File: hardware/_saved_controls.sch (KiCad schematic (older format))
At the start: 25 parts, among them J301 PJ301M-12, J302 PJ301M-12, J303 PJ301M-12, J304 PJ301M-12, U301 MCP6004

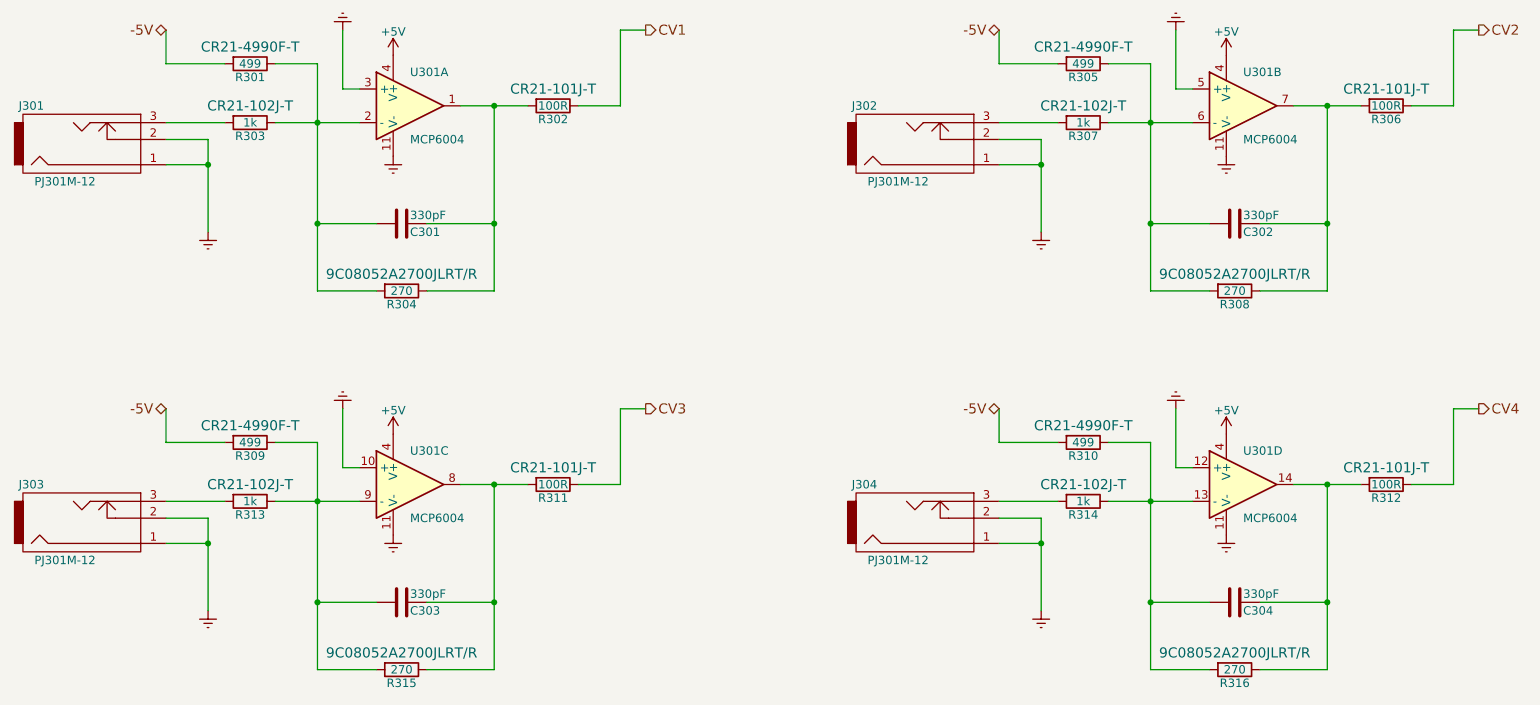
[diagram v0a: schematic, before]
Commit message: jacks on a different sheet than the buffers. single PCB with jumpers and mouse bites
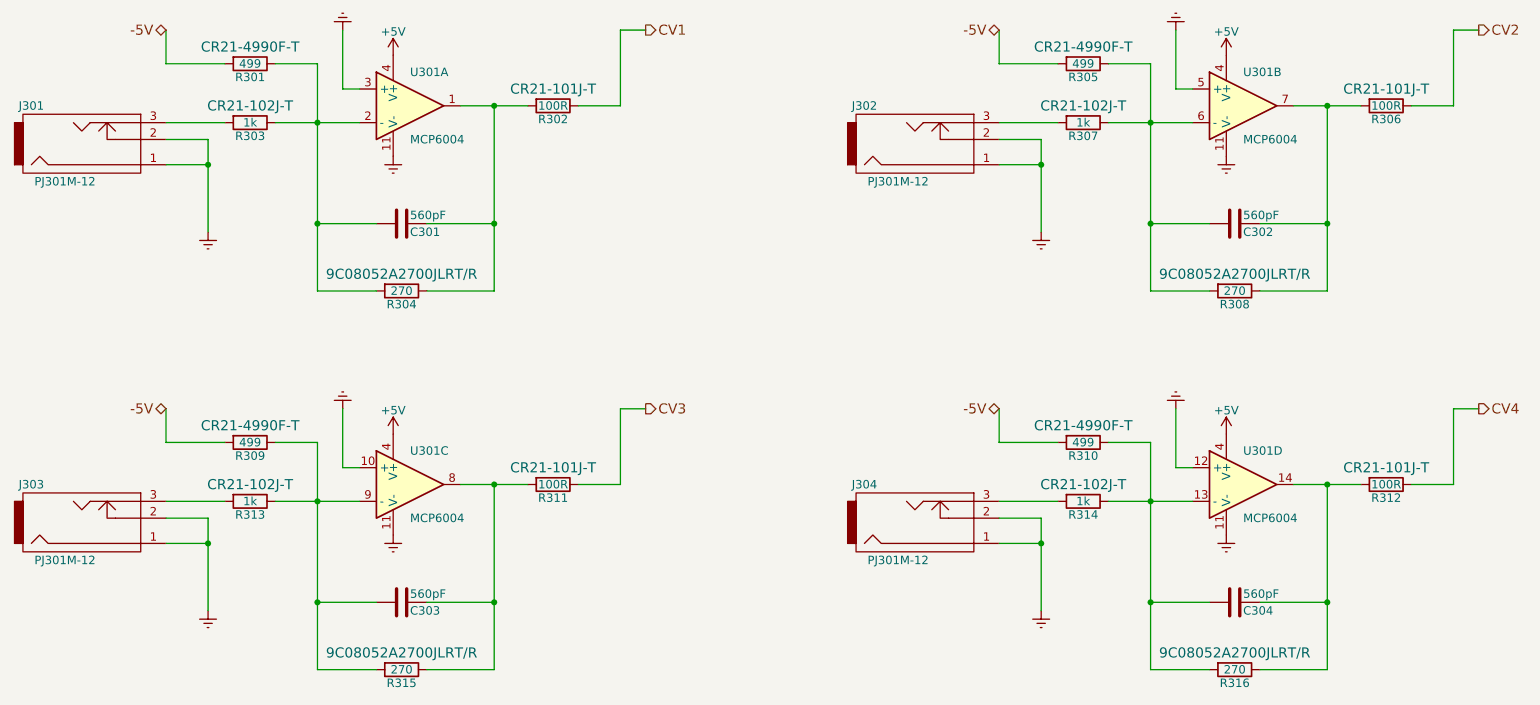
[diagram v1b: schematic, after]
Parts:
- C301, C302, C303, C304: value 330pF -> 560pF; footprint (none) -> Capacitors_THT:C_Axial_L3.8mm_D2.6mm_P7.50mm_Horizontal
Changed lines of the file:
@@
 P 3400 2300
 F 0 "C301" V 3450 2350 50  0000 L CNN
-F 1 "330pF" V 3350 2350 50  0000 L CNN
-F 2 "" H 3438 2150 50  0000 C CNN
+F 1 "560pF" V 3350 2350 50  0000 L CNN
+F 2 "Capacitors_THT:C_Axial_L3.8mm_D2.6mm_P7.50mm_Horizontal" H 3438 2150 50  0001 C CNN
 F 3 "" H 3400 2300 50  0000 C CNN
 	1    3400 2300
@@
 P 8350 2300
 F 0 "C302" V 8400 2350 50  0000 L CNN
-F 1 "330pF" V 8300 2350 50  0000 L CNN
-F 2 "" H 8388 2150 50  0000 C CNN
+F 1 "560pF" V 8300 2350 50  0000 L CNN
+F 2 "Capacitors_THT:C_Axial_L3.8mm_D2.6mm_P7.50mm_Horizontal" H 8388 2150 50  0001 C CNN
 F 3 "" H 8350 2300 50  0000 C CNN
 	1    8350 2300
@@
 P 3400 4550
 F 0 "C303" V 3450 4600 50  0000 L CNN
-F 1 "330pF" V 3350 4600 50  0000 L CNN
-F 2 "" H 3438 4400 50  0000 C CNN
+F 1 "560pF" V 3350 4600 50  0000 L CNN
+F 2 "Capacitors_THT:C_Axial_L3.8mm_D2.6mm_P7.50mm_Horizontal" H 3438 4400 50  0001 C CNN
 F 3 "" H 3400 4550 50  0000 C CNN
 	1    3400 4550
@@
 P 8350 4550
 F 0 "C304" V 8400 4600 50  0000 L CNN
-F 1 "330pF" V 8300 4600 50  0000 L CNN
-F 2 "" H 8388 4400 50  0000 C CNN
+F 1 "560pF" V 8300 4600 50  0000 L CNN
+F 2 "Capacitors_THT:C_Axial_L3.8mm_D2.6mm_P7.50mm_Horizontal" H 8388 4400 50  0001 C CNN
 F 3 "" H 8350 4550 50  0000 C CNN
 	1    8350 4550
